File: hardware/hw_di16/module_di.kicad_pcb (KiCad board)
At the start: 2 copper layers, 89.5 x 62.2 mm, 119 parts, among them P1 DEBUG, P2 DI_0, P3 DI_1, P4 MOD_IN, U1 STM32F103C8Tx, U2 TLP291-4, U3 TLP291-4, U4 TLP291-4, U5 TLP291-4

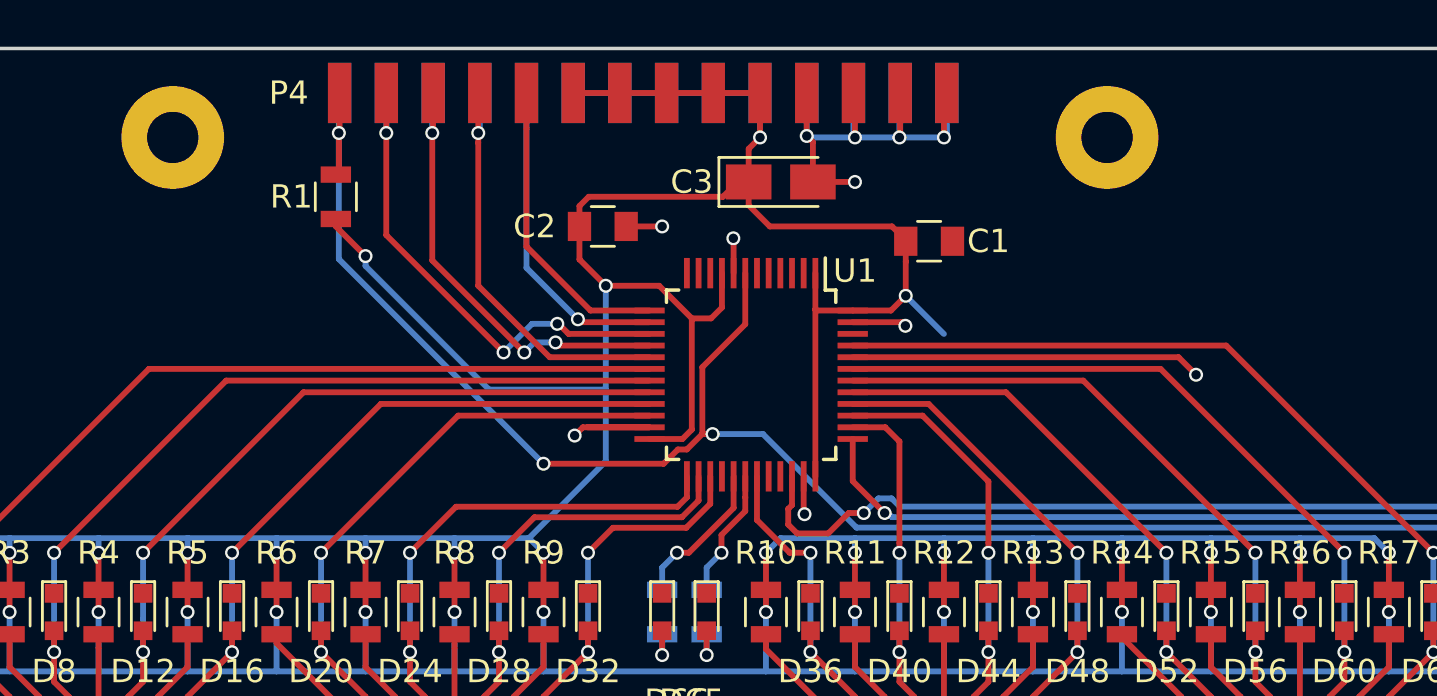
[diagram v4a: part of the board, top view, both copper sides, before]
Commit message: Обновлены платы модулей.
Добавлен разъем для работы с аппаратным загрузчиком.
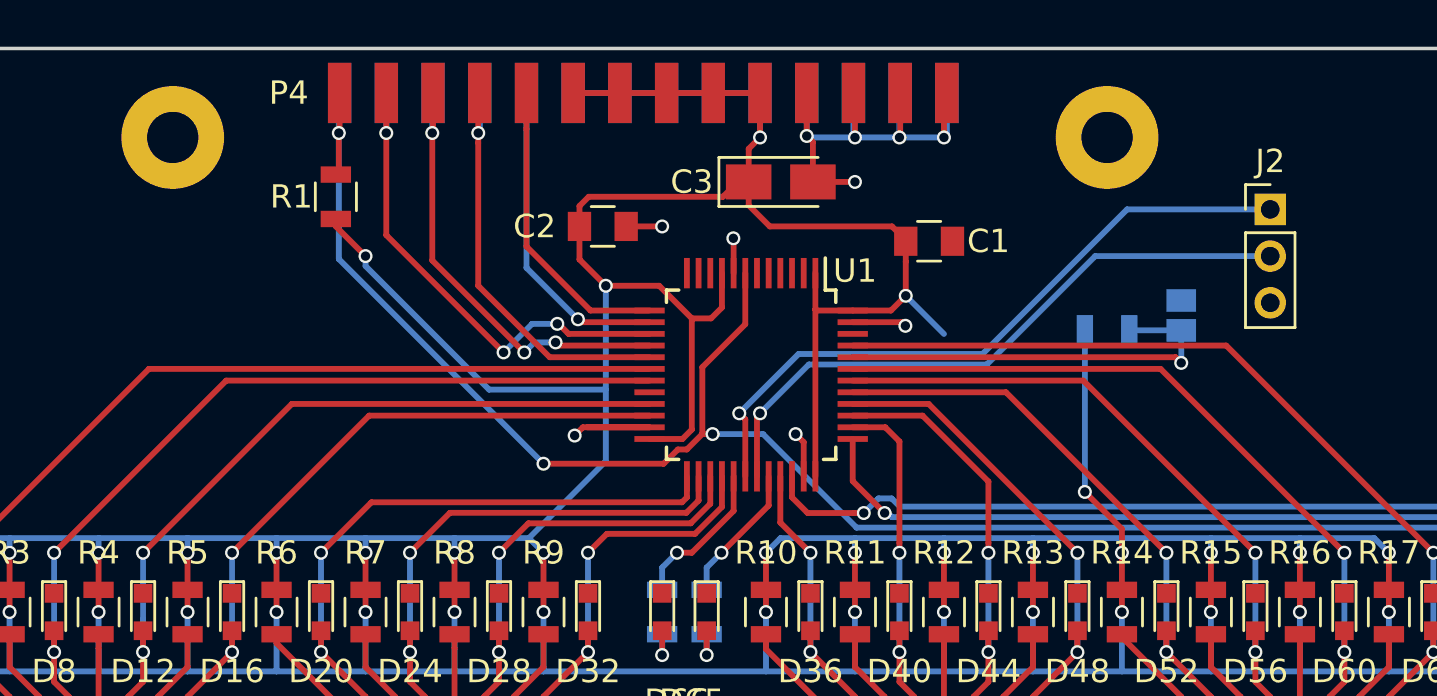
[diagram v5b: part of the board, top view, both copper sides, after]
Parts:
- added J1: BOOT0, Connect:GS2, B.Cu at (167.6, 74.3)
- added J2: UART1, Pin_Headers:Pin_Header_Straight_1x03_Pitch2.00mm, F.Cu at (171.4, 69.8)
- added R20: 10k, Resistors_SMD:R_0805, B.Cu at (164.5, 74.9)
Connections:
- C1 pad 2: VSS -> BOOT1
- C2 pad 2: VSS -> BOOT1
- C3 pad 2: VSS -> BOOT1
- D12 pad 1: VSS -> BOOT1
- D16 pad 1: VSS -> BOOT1
- D20 pad 1: VSS -> BOOT1
- D24 pad 1: VSS -> BOOT1
- D28 pad 1: VSS -> BOOT1
- D32 pad 1: VSS -> BOOT1
- D36 pad 1: VSS -> BOOT1
- D4 pad 1: VSS -> BOOT1
- D40 pad 1: VSS -> BOOT1
- D44 pad 1: VSS -> BOOT1
- D48 pad 1: VSS -> BOOT1
- D52 pad 1: VSS -> BOOT1
- D56 pad 1: VSS -> BOOT1
- D60 pad 1: VSS -> BOOT1
- D64 pad 1: VSS -> BOOT1
- D65 pad 1: VSS -> BOOT1
- D66 pad 1: VSS -> BOOT1
- D8 pad 1: VSS -> BOOT1
- P1 pad 5: VSS -> BOOT1
- P4 pad 21: VSS -> BOOT1
- P4 pad 22: VSS -> BOOT1
- P4 pad 23: VSS -> BOOT1
- P4 pad 24: VSS -> BOOT1
- P4 pad 25: VSS -> BOOT1
- P4 pad 26: VSS -> BOOT1
- P4 pad 27: VSS -> BOOT1
- P4 pad 28: VSS -> BOOT1
- U1 pad 20: DI2 -> BOOT1
- U1 pad 21: DI3 -> DI2
- U1 pad 22: DI4 -> DI3
- U1 pad 23: VSS -> BOOT1
- U1 pad 25: DI5 -> DI4
- U1 pad 26: DI6 -> DI5
- U1 pad 27: DI7 -> DI6
- U1 pad 28: Net-(U1-Pad28) -> DI7
- U1 pad 30: SOK -> TX
- U1 pad 31: DI8 -> RX
- U1 pad 32: Net-(U1-Pad32) -> SOK
- U1 pad 33: Net-(U1-Pad33) -> DI8
- U1 pad 35: VSS -> BOOT1
- U1 pad 44: VSS -> BOOT0
- U1 pad 47: VSS -> BOOT1
- U1 pad 8: VSS -> BOOT1
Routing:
- net VSS: track 53.1 -> 0.00 mm, vias 11 -> 0
- net BOOT1: track 0.00 -> 38.4 mm, vias 0 -> 10
- net TX: track 0.00 -> 29.2 mm, vias 0 -> 1
- net RX: track 0.00 -> 27.4 mm, vias 0 -> 1
- net BOOT0: track 0.00 -> 17.8 mm, vias 0 -> 1
- net VDD: track 317.9 -> 328.2 mm, vias 36 -> 37
- net SWDIO: track 40.1 -> 38.4 mm
- net DI4: track 25.2 -> 26.2 mm
- net DI8: track 13.4 -> 12.5 mm
- net DI5: track 21.9 -> 22.5 mm
- net DI7: track 16.0 -> 16.5 mm
- net DI6: track 18.7 -> 19.2 mm
- added copper zone on B.Cu, net BOOT1
- added copper zone on F.Cu, net BOOT1
- removed copper zone on B.Cu, net VSS
- removed copper zone on F.Cu, net VSS

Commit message: Обновлены платы модулей
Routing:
- net BOOT1: track 38.4 -> 95.9 mm, vias 10 -> 15
- net VDD: track 328.2 -> 325.8 mm, vias 37 -> 36
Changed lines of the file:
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@@
   (general
     (links 272)
-    (no_connects 86)
-    (area 99.619999 62.789999 189.305001 125.170001)
+    (no_connects 1)
+    (area 86.106667 53.245 206.628334 132.175001)
     (thickness 1.6)
     (drawings 27)
-    (tracks 820)
+    (tracks 846)
     (zones 0)
     (modules 122)
@@
     (visible_elements 7FFFFFFF)
     (pcbplotparams
-      (layerselection 0x010f0_ffffffff)
+      (layerselection 0x010f0_80000001)
       (usegerberextensions false)
       (excludeedgelayer true)
@@
   (segment (start 163.515 81.854) (end 163.576 81.915) (width 0.25) (layer B.Cu) (net 1))
   (via (at 163.5125 81.8515) (size 0.6) (drill 0.4) (layers F.Cu B.Cu) (net 1))
-  (segment (start 157.48 75.0885) (end 155.845 73.4535) (width 0.25) (layer B.Cu) (net 1))
   (segment (start 143.002 73.025) (end 143.002 77.47) (width 0.25) (layer B.Cu) (net 1))
   (segment (start 132.715 71.755) (end 132.715 72.179264) (width 0.25) (layer B.Cu) (net 1))
@@
   (segment (start 113.665 84.455) (end 114.290001 83.829999) (width 0.25) (layer B.Cu) (net 1))
   (segment (start 139.709999 83.829999) (end 140.335 84.455) (width 0.25) (layer B.Cu) (net 1))
-  (via (at 155.845 73.4535) (size 0.6) (drill 0.4) (layers F.Cu B.Cu) (net 1))
   (segment (start 172.72 83.829999) (end 168.91 83.829999) (width 0.25) (layer B.Cu) (net 1))
   (segment (start 175.904999 83.829999) (end 172.72 83.829999) (width 0.25) (layer B.Cu) (net 1))
@@
   (via (at 146.05 84.455) (size 0.6) (drill 0.4) (layers F.Cu B.Cu) (net 103))
   (segment (start 145.415 85.09) (end 146.05 84.455) (width 0.25) (layer B.Cu) (net 103))
+  (segment (start 151.13 79.375) (end 156.083 79.375) (width 0.25) (layer B.Cu) (net 105))
+  (segment (start 156.083 79.375) (end 156.5275 79.8195) (width 0.25) (layer B.Cu) (net 105))
+  (via (at 156.5275 79.8195) (size 0.6) (drill 0.4) (layers F.Cu B.Cu) (net 105))
+  (segment (start 143.8275 85.725) (end 143.8275 81.534) (width 0.25) (layer B.Cu) (net 105))
+  (segment (start 143.8275 81.534) (end 143.7005 81.407) (width 0.25) (layer B.Cu) (net 105))
+  (segment (start 145.415 86.195) (end 144.2975 86.195) (width 0.25) (layer F.Cu) (net 105))
+  (segment (start 144.2975 86.195) (end 143.8275 85.725) (width 0.25) (layer F.Cu) (net 105))
+  (via (at 143.8275 85.725) (size 0.6) (drill 0.4) (layers F.Cu B.Cu) (net 105))
+  (segment (start 146.05 77.47) (end 146.05 79.0575) (width 0.25) (layer B.Cu) (net 105))
+  (segment (start 146.05 79.0575) (end 143.7005 81.407) (width 0.25) (layer B.Cu) (net 105))
+  (segment (start 155.829 74.7395) (end 148.7805 74.7395) (width 0.25) (layer B.Cu) (net 105))
+  (segment (start 148.7805 74.7395) (end 146.05 77.47) (width 0.25) (layer B.Cu) (net 105))
+  (segment (start 153.67 68.58) (end 153.67 72.5805) (width 0.25) (layer B.Cu) (net 105))
+  (segment (start 153.67 72.5805) (end 155.829 74.7395) (width 0.25) (layer B.Cu) (net 105))
+  (segment (start 148.463 70.993) (end 151.257 70.993) (width 0.25) (layer B.Cu) (net 105))
+  (segment (start 151.257 70.993) (end 153.67 68.58) (width 0.25) (layer B.Cu) (net 105))
+  (segment (start 145.415 70.485) (end 147.955 70.485) (width 0.25) (layer F.Cu) (net 105))
+  (segment (start 147.955 70.485) (end 148.463 70.993) (width 0.25) (layer F.Cu) (net 105))
+  (segment (start 141.0335 81.407) (end 143.7005 81.407) (width 0.25) (layer F.Cu) (net 105))
+  (via (at 143.7005 81.407) (size 0.6) (drill 0.4) (layers F.Cu B.Cu) (net 105))
+  (segment (start 141.6685 79.4385) (end 141.6685 80.772) (width 0.25) (layer B.Cu) (net 105))
+  (segment (start 141.6685 80.772) (end 141.0335 81.407) (width 0.25) (layer B.Cu) (net 105))
+  (via (at 141.0335 81.407) (size 0.6) (drill 0.4) (layers F.Cu B.Cu) (net 105))
+  (segment (start 145.415 70.485) (end 145.415 76.835) (width 0.25) (layer B.Cu) (net 105))
+  (segment (start 145.415 76.835) (end 146.05 77.47) (width 0.25) (layer B.Cu) (net 105))
+  (segment (start 144.875 77.585) (end 145.935 77.585) (width 0.25) (layer F.Cu) (net 105))
+  (segment (start 145.935 77.585) (end 146.05 77.47) (width 0.25) (layer F.Cu) (net 105))
+  (via (at 146.05 77.47) (size 0.6) (drill 0.4) (layers F.Cu B.Cu) (net 105))
   (segment (start 151.475 81.185) (end 151.475 79.72) (width 0.25) (layer F.Cu) (net 105))
   (segment (start 151.475 79.72) (end 151.13 79.375) (width 0.25) (layer F.Cu) (net 105))
